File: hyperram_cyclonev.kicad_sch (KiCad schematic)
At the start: 57 parts, among them IC1 AP63205WU, IC2 TXB0108PWR, IC3 S26KL128SDABHI020, IC4 W25Q32JVSSIQ_TR, IC5 S27KL0641DABHI020, J1 ASP-122952-01, J2 HDMI_A, J3 Conn_02x10_Odd_Even, J4 Conn_02x06_Odd_Even, J5 Conn_02x06_Top_Bottom, J6 Conn_02x06_Top_Bottom, J7 Conn_02x06_Top_Bottom, Q1 BSS138, Q2 BSS138

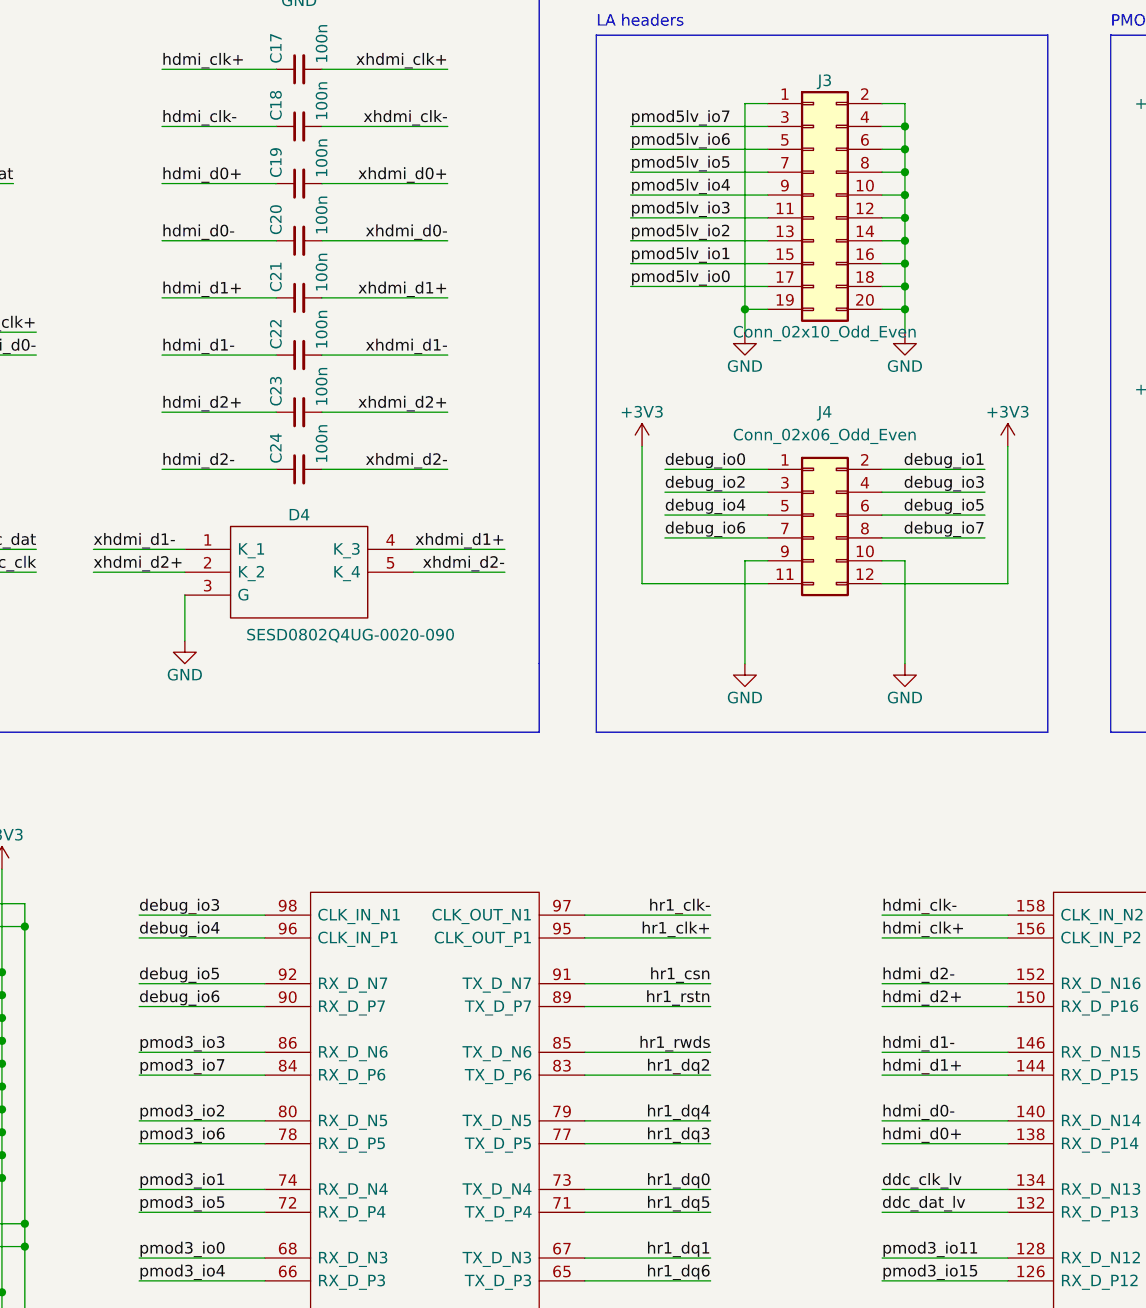
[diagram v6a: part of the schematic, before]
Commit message: Changed order of HDMI data signals to avoid crossing
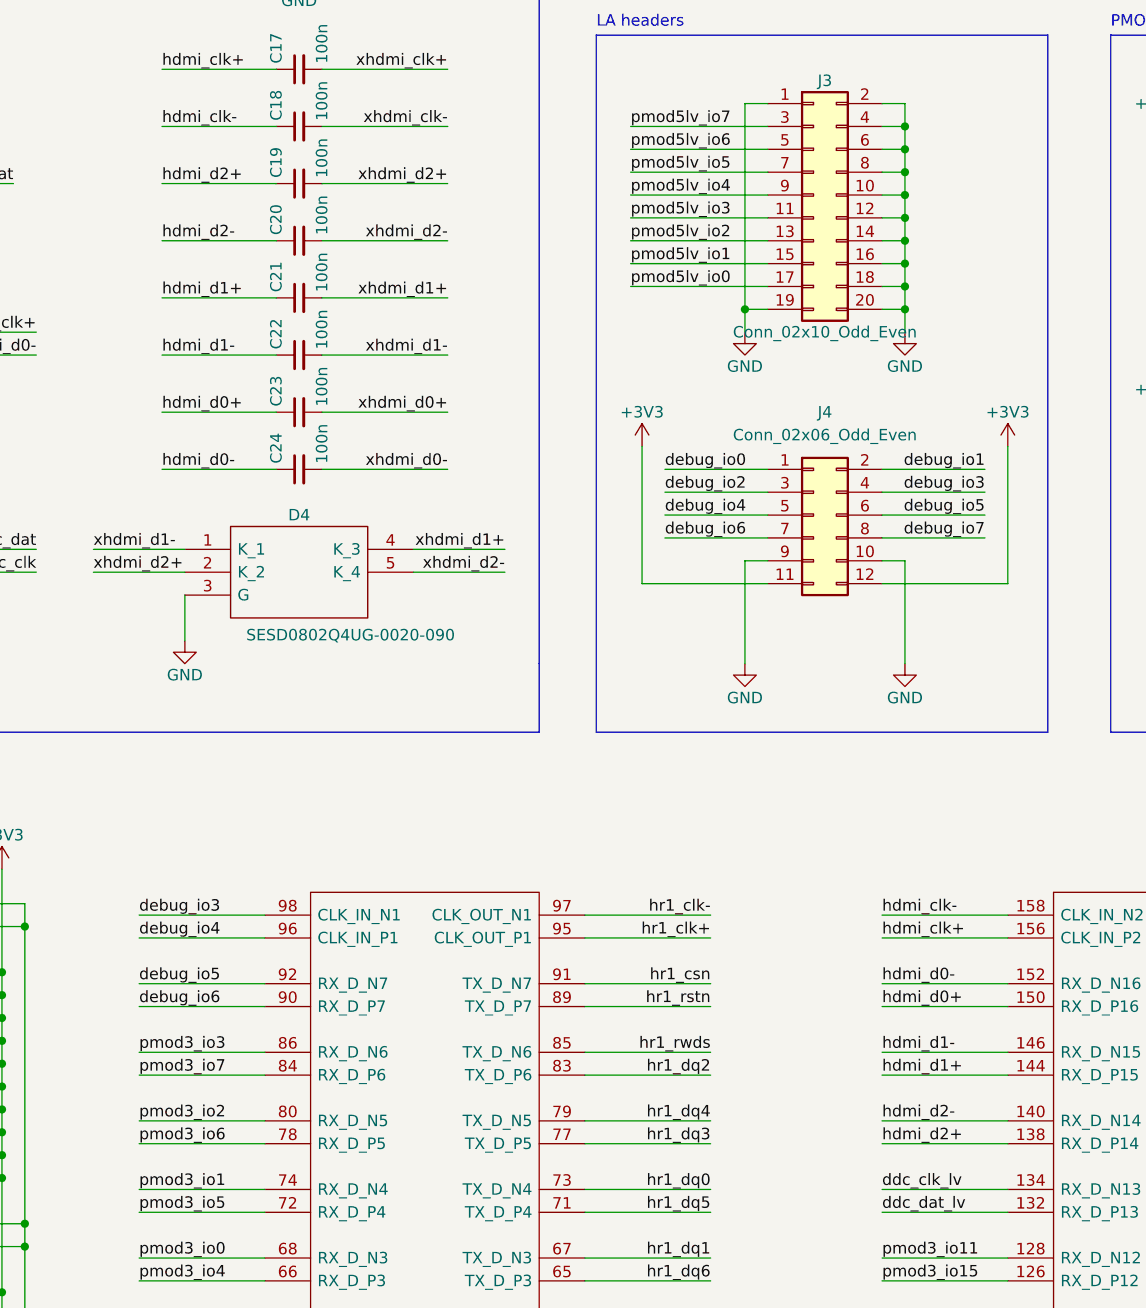
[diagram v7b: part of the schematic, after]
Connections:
- net hdmi_d0+: now also C23.1, J1.150 (RX_D_P16); no longer C19.1, J1.138 (RX_D_P14)
- net hdmi_d0-: now also C24.1, J1.152 (RX_D_N16); no longer C20.1, J1.140 (RX_D_N14)
- net hdmi_d2+: now also C19.1, J1.138 (RX_D_P14); no longer C23.1, J1.150 (RX_D_P16)
- net hdmi_d2-: now also C20.1, J1.140 (RX_D_N14); no longer C24.1, J1.152 (RX_D_N16)
- net xhdmi_d0+: now also C23.2; no longer C19.2
- net xhdmi_d0-: now also C24.2; no longer C20.2
- net xhdmi_d2+: now also C19.2; no longer C23.2
- net xhdmi_d2-: now also C20.2; no longer C24.2
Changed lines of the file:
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@@
 	)
 	(label "xhdmi_d0+"
-		(at 110.49 111.76 180)
+		(at 110.49 137.16 180)
 		(fields_autoplaced yes)
 		(effects
@@
 	)
 	(label "hdmi_d2+"
-		(at 158.75 203.2 0)
+		(at 158.75 218.44 0)
 		(fields_autoplaced yes)
 		(effects
@@
 	)
 	(label "hdmi_d0+"
-		(at 78.74 111.76 0)
+		(at 78.74 137.16 0)
 		(fields_autoplaced yes)
 		(effects
@@
 	)
 	(label "xhdmi_d0-"
-		(at 110.49 118.11 180)
+		(at 110.49 143.51 180)
 		(fields_autoplaced yes)
 		(effects
@@
 	)
 	(label "xhdmi_d2-"
-		(at 110.49 143.51 180)
+		(at 110.49 118.11 180)
 		(fields_autoplaced yes)
 		(effects
@@
 	)
 	(label "xhdmi_d2+"
-		(at 110.49 137.16 180)
+		(at 110.49 111.76 180)
 		(fields_autoplaced yes)
 		(effects
@@
 	)
 	(label "hdmi_d0+"
-		(at 158.75 218.44 0)
+		(at 158.75 203.2 0)
 		(fields_autoplaced yes)
 		(effects
@@
 	)
 	(label "hdmi_d0-"
-		(at 158.75 215.9 0)
+		(at 158.75 200.66 0)
 		(fields_autoplaced yes)
 		(effects
@@
 	)
 	(label "hdmi_d2+"
-		(at 78.74 137.16 0)
+		(at 78.74 111.76 0)
 		(fields_autoplaced yes)
 		(effects
@@
 	)
 	(label "hdmi_d2-"
-		(at 78.74 143.51 0)
+		(at 78.74 118.11 0)
 		(fields_autoplaced yes)
 		(effects
@@
 	)
 	(label "hdmi_d2-"
-		(at 158.75 200.66 0)
+		(at 158.75 215.9 0)
 		(fields_autoplaced yes)
 		(effects
@@
 	)
 	(label "hdmi_d0-"
-		(at 78.74 118.11 0)
-		(fields_autoplaced yes)
-		(effects
+		(at 78.74 143.51 0)
+		(fields_autoplaced yes)
+		(effects

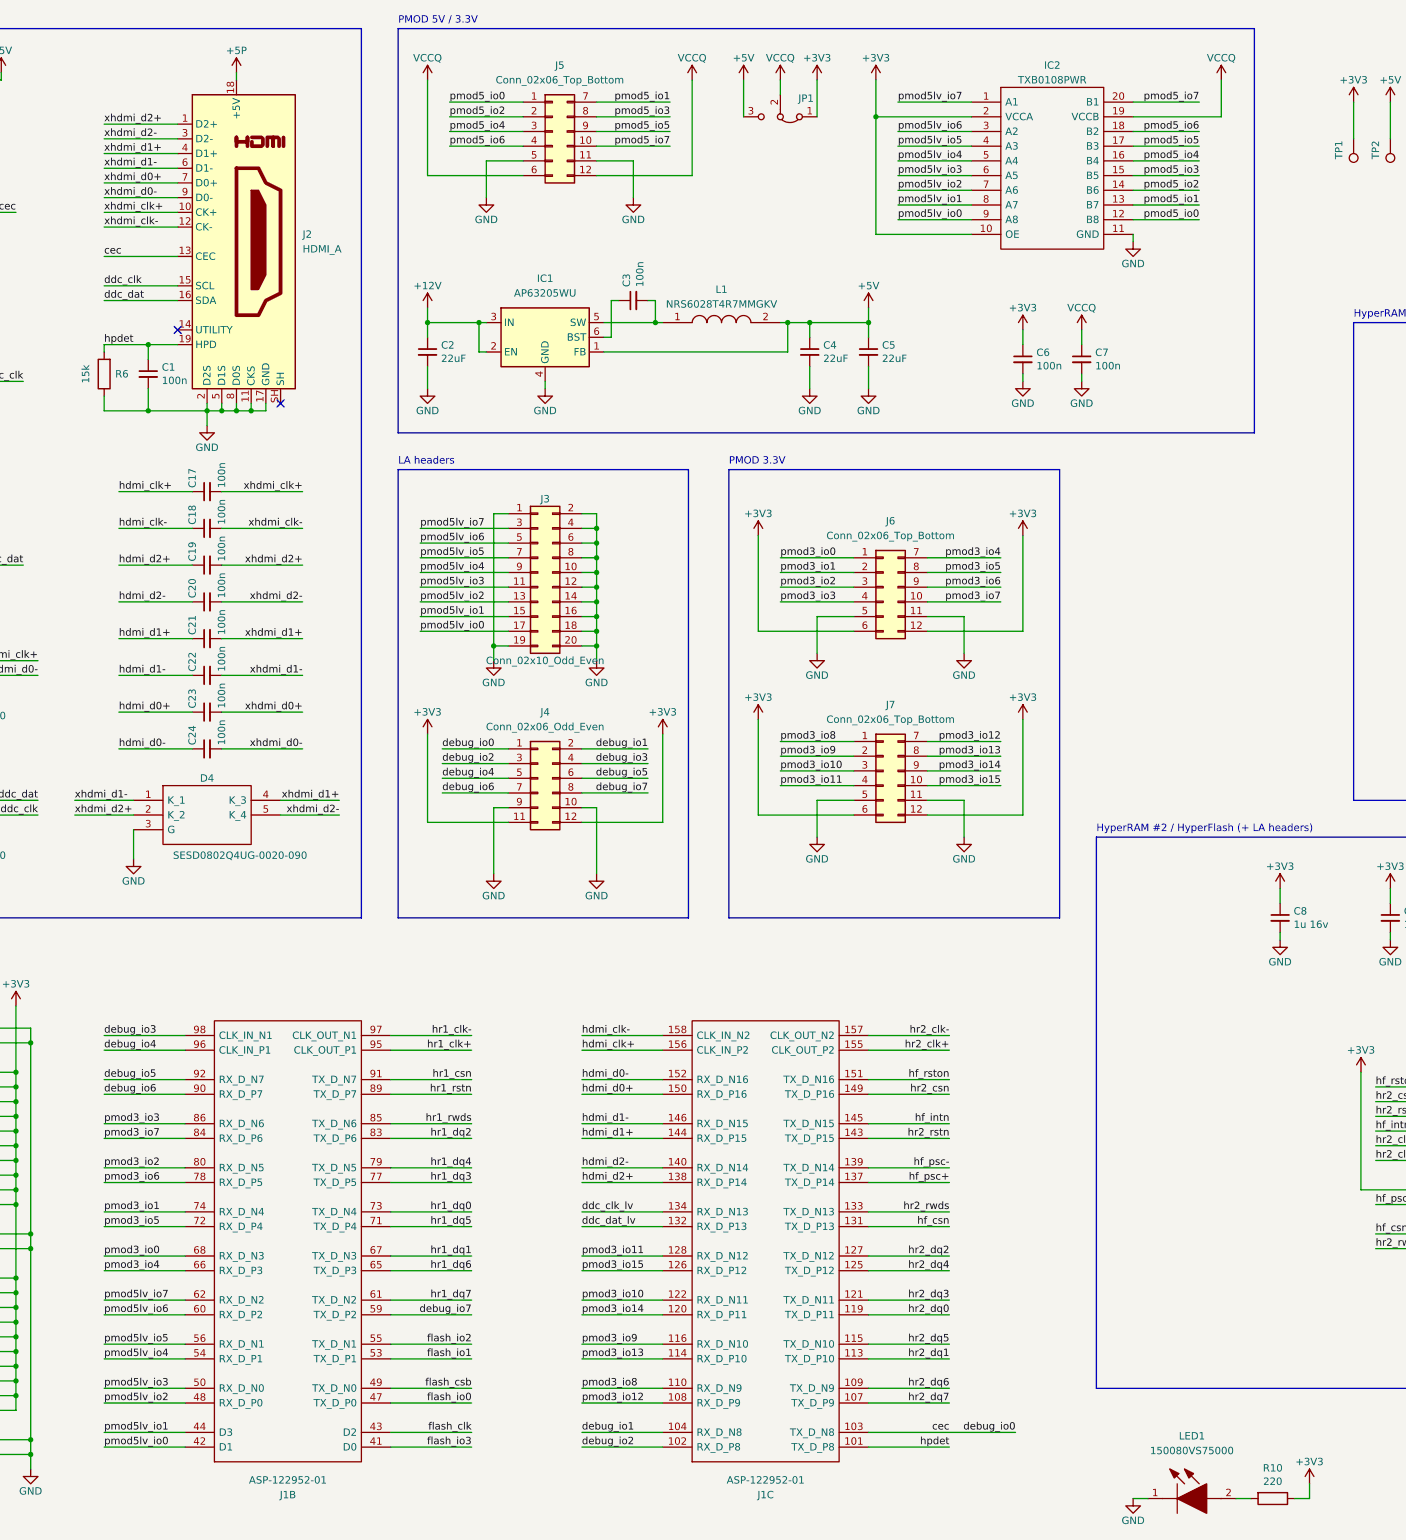
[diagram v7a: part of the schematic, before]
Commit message: Added additional resistors on LA / PMOD path
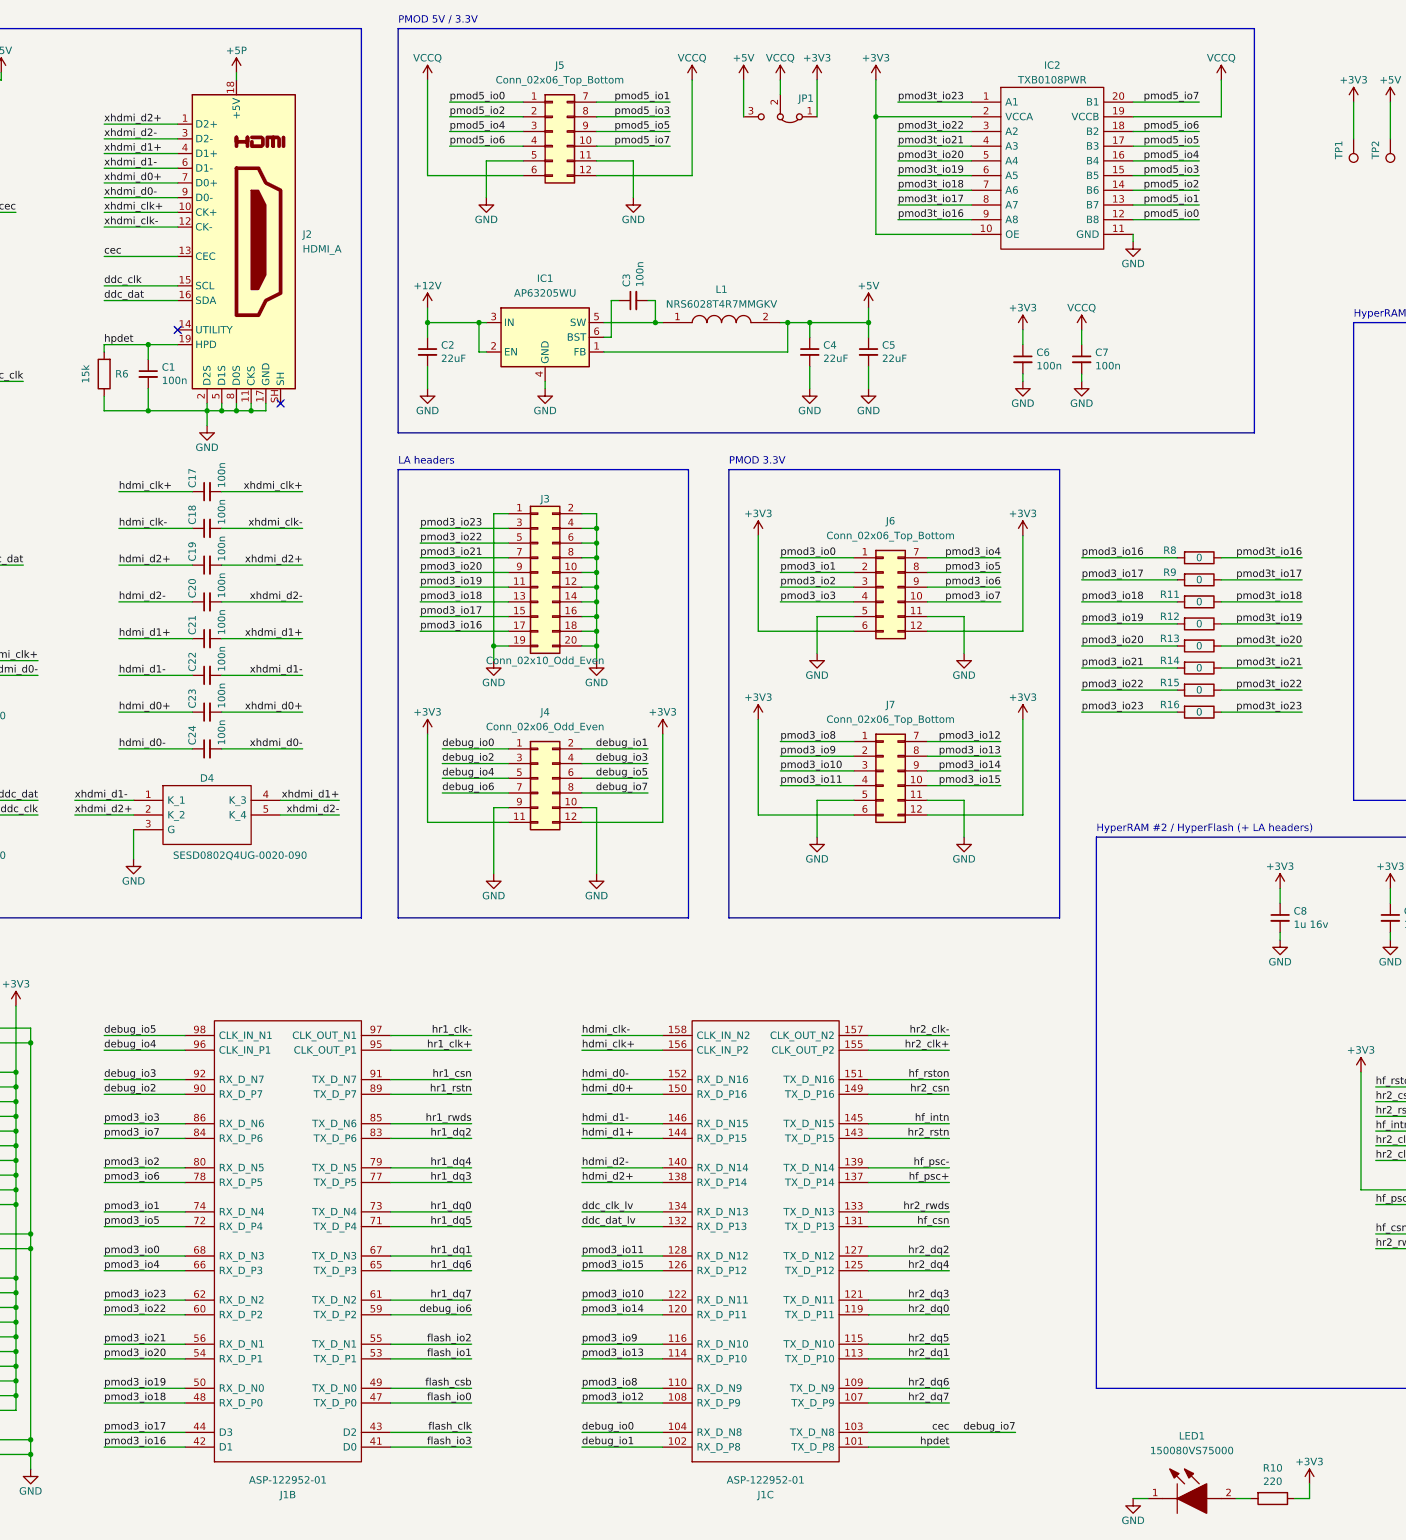
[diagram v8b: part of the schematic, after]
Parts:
- added R11, R12, R13, R14, R15, R16, R8, R9: 0, Resistor_SMD:R_0402_1005Metric_Pad0.72x0.64mm_HandSolder, symbol Device:R
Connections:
- net cec: now also J4.8 (Pin_8); no longer J4.1 (Pin_1)
- net debug_io1: now also J1.102 (RX_D_P8); no longer J1.104 (RX_D_N8)
- net debug_io2: now also J1.90 (RX_D_P7); no longer J1.102 (RX_D_P8)
- net debug_io3: now also J1.92 (RX_D_N7); no longer J1.98 (CLK_IN_N1)
- net debug_io5: now also J1.98 (CLK_IN_N1); no longer J1.92 (RX_D_N7)
- net debug_io6: now also J1.59 (TX_D_P2); no longer J1.90 (RX_D_P7)
- removed net debug_io7: J1.59 (TX_D_P2), J4.8 (Pin_8)
- net pmod5lv_io0 renamed pmod3_io16
- net pmod3_io16: now also R8.2; no longer IC2.9 (A8)
- net pmod5lv_io1 renamed pmod3_io17
- net pmod3_io17: now also R9.2; no longer IC2.8 (A7)
- net pmod5lv_io2 renamed pmod3_io18
- net pmod3_io18: now also R11.2; no longer IC2.7 (A6)
- net pmod5lv_io3 renamed pmod3_io19
- net pmod3_io19: now also R12.2; no longer IC2.6 (A5)
- net pmod5lv_io4 renamed pmod3_io20
- net pmod3_io20: now also R13.2; no longer IC2.5 (A4)
- net pmod5lv_io5 renamed pmod3_io21
- net pmod3_io21: now also R14.2; no longer IC2.4 (A3)
- net pmod5lv_io6 renamed pmod3_io22
- net pmod3_io22: now also R15.2; no longer IC2.3 (A2)
- net pmod5lv_io7 renamed pmod3_io23
- net pmod3_io23: now also R16.2; no longer IC2.1 (A1)
- new net debug_io0: J1.104 (RX_D_N8), J4.1 (Pin_1)
- new net pmod3t_io16: IC2.9 (A8), R8.1
- new net pmod3t_io17: IC2.8 (A7), R9.1
- new net pmod3t_io18: IC2.7 (A6), R11.1
- new net pmod3t_io19: IC2.6 (A5), R12.1
- new net pmod3t_io20: IC2.5 (A4), R13.1
- new net pmod3t_io21: IC2.4 (A3), R14.1
- new net pmod3t_io22: IC2.3 (A2), R15.1
- new net pmod3t_io23: IC2.1 (A1), R16.1
